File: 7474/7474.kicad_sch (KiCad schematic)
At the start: 45 parts, among them J1 USB, J10 Conn_02x03_Odd_Even, J11 Conn_02x03_Odd_Even, J12 Conn_02x03_Odd_Even, J13 Conn_02x03_Odd_Even, J14 Conn_02x03_Odd_Even, J15 Conn_02x03_Odd_Even, J16 Conn_02x03_Odd_Even, J17 Conn_02x03_Odd_Even, J18 Conn_02x03_Odd_Even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

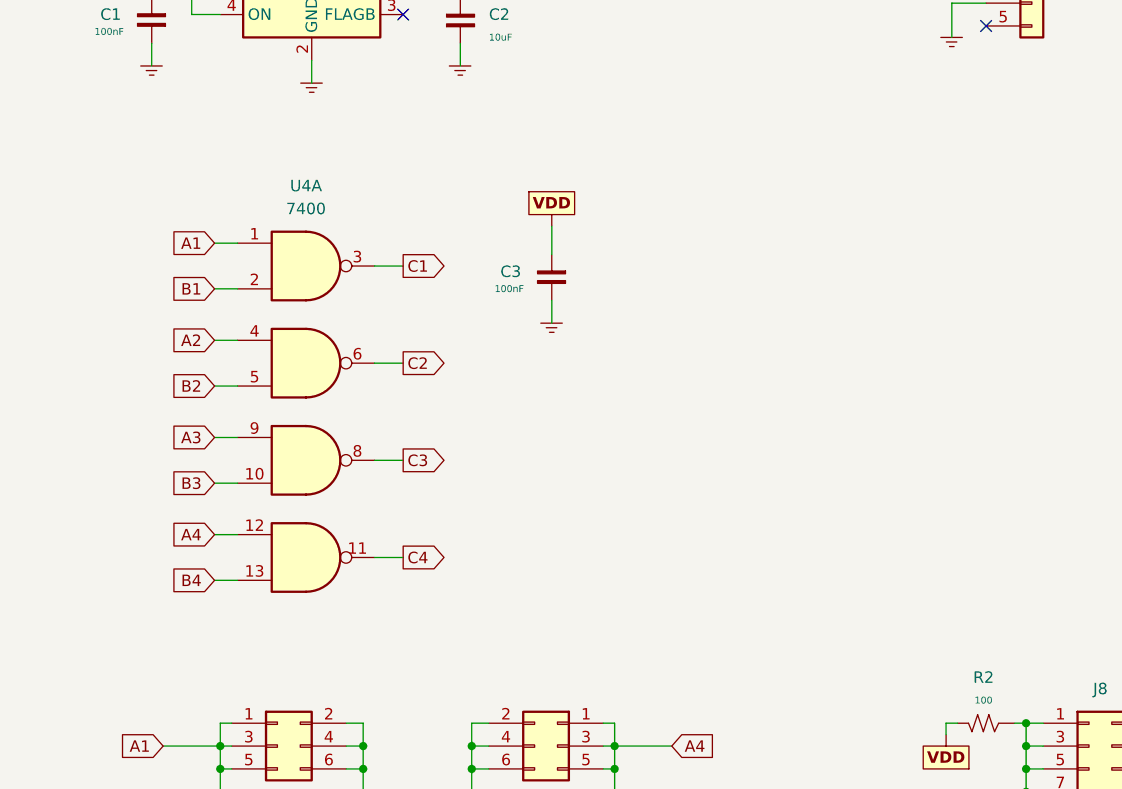
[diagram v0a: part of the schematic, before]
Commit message: Simplificação do circuito. Inclusão da placa 7474.
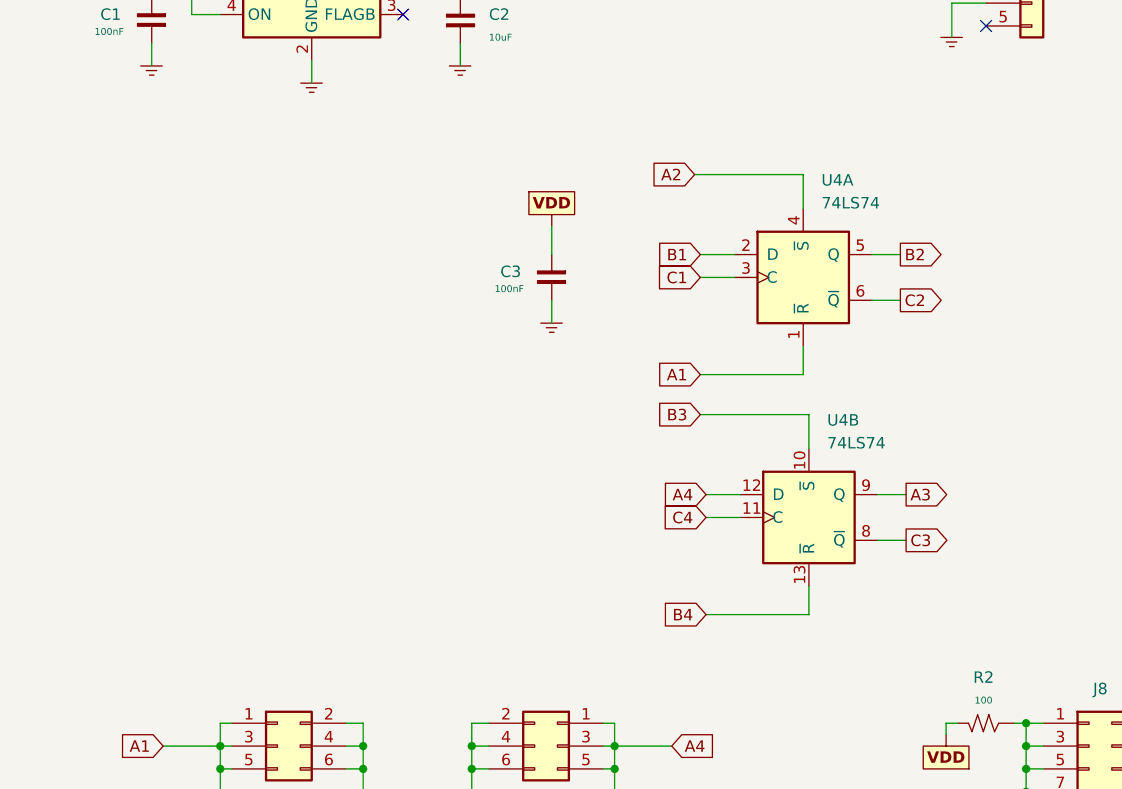
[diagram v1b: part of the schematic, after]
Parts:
- removed U4: 7400, Package_SO:SO-14_3.9x8.65mm_P1.27mm, symbol 74xx:7400
- added U4: 74LS74, symbol 74xx:74LS74
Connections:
- net A1: now also U4.1 (~{R})
- net A2: now also U4.4 (~{S})
- net A3: now also U4.9 (Q)
- net A4: now also U4.12 (D)
- net B1: now also U4.2 (D)
- net B2: now also U4.5 (Q)
- net B3: now also U4.10 (~{S})
- net B4: now also U4.13 (~{R})
- net C1: now also U4.3 (C)
- net C2: now also U4.6 (~{Q})
- net C3: now also U4.8 (~{Q})
- net C4: now also U4.11 (C)
